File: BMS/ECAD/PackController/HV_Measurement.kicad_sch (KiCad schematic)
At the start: 0 parts

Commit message: implement HV measurement
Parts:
- added C28, C29, C30, C35, C40, C41: 1uC 0805 50V, symbol Device:C
- added C31, C39, C42: 100n 0603 50V, symbol Device:C
- added C32, C36: 100nF 0603 100V, Capacitor_SMD:C_0603_1608Metric_Pad1.08x0.95mm_HandSolder, symbol Device:C
- added C33, C34, C37, C38: 10uF 0805 50V, Capacitor_SMD:C_0805_2012Metric, symbol Device:C
- added R49, R59, R63, R64: 4.7MR 2512 3kV 1%, symbol Device:R
- added R60: 55.6kR 2512 500V 1%, symbol Device:R
- added R61, R62, R66, R67, R70: 10kR, Resistor_SMD:R_0603_1608Metric_Pad0.98x0.95mm_HandSolder, symbol Device:R
- added R65: 39kR 2512 500V 1%, symbol Device:R
- added R68: 68K 1%, Resistor_SMD:R_0603_1608Metric_Pad0.98x0.95mm_HandSolder, symbol Device:R
- added R69: 3.3k 1%, Resistor_SMD:R_0603_1608Metric_Pad0.98x0.95mm_HandSolder, symbol Device:R
- added U10, U12: (no value), symbol EKartParts:ADUM3190
- added U11, U13: TEA1-0505HI, Converter_DCDC:Converter_DCDC_TRACO_TEA1-xxxxHI_THT, symbol Converter_DCDC:TEA1-0505HI
- added U14: (no value), symbol EKartParts:ADCMP393ARUZ
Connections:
- new net: C38.2, U13.2 (-Vin)
- new net: C35.1, U12.14 (VREG2)
- new net: R61.1, R62.2, U10.6 (EAOUT2)
- new net: C28.1, U10.14 (VREG2)
- new net: C34.2, U11.2 (-Vin)
- new net: C32.1, C33.2, U11.5 (-Vout)
- new net: R63.2, R64.1
- new net: C36.1, C37.2, U13.5 (-Vout)
- new net: C30.1, U10.3 (VREG1)
- new net: R68.2, R69.1, U14.5 (+)
- new net: C42.1, U14.3 (VCC)
- new net: R66.1, R67.2, U12.6 (EAOUT2)
- new net: R49.2, R59.1
- new net: U12.10 (COMP), U12.11 (-In)
- new net: C40.1, U12.3 (VREG1)
- new net: U10.10 (COMP), U10.11 (-In)
- new net +3.3V: C29.1, C41.1, R61.2, R66.2, R68.1, R70.1, U10.1 (VDD1), U12.1 (VDD1)
- new net +5V: C34.1, C38.1, U11.1 (+Vin), U13.1 (+Vin)
- new net +5V_ACCU: C36.2, C37.1, U12.16 (VDD2), U13.7 (+Vout)
- new net +5V_VEHI: C32.2, C33.1, U10.16 (VDD2), U11.7 (+Vout)
- new net DANGER_V: R70.2, U14.2
- new net GND: C29.2, C30.2, C31.2, C39.2, C40.2, C41.2, C42.2, R69.2, U10.2 (GND1), U10.8 (GND1), U12.2 (GND1), U12.8 (GND1), U14.12 (GND)
- new net TS_P_ACCU: C35.2, R63.1, R64.2, R65.1, R65.2, U12.12 (+IN), U12.15 (GND2), U12.9 (GND2)
- new net TS_P_VEHI: C28.2, R49.1, R59.2, R60.1, R60.2, U10.12 (+IN), U10.15 (GND2), U10.9 (GND2)
- new net V_ACCU: C39.1, R67.1
- new net V_VEHI: C31.1, R62.1, U14.4 (-)
- no-connect marks 0 -> 6

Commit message: schematic finished, review tbd
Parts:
- removed unit 4 of U14
- removed unit 3 of U14
- added R76: 68K 1%, Resistor_SMD:R_0603_1608Metric_Pad0.98x0.95mm_HandSolder, symbol Device:R
- added R82: 3.3k 1%, Resistor_SMD:R_0603_1608Metric_Pad0.98x0.95mm_HandSolder, symbol Device:R
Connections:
- net +3.3V: now also R76.1
- net DANGER_V: now also U14.1; no longer R70.2, U14.2
- net GND: now also R82.2
- net TS_P_ACCU: no longer C35.2, R64.2, R65.1, R65.2, U12.12 (+IN), U12.15 (GND2), U12.9 (GND2)
- net TS_P_VEHI: no longer C28.2, R59.2, R60.1, R60.2, U10.12 (+IN), U10.15 (GND2), U10.9 (GND2)
- net V_VEHI: now also U14.7 (+)
- net TS_N_VEHI: now reaches C32.1, C33.2, U11.5 (-Vout)
- net TS_N_VEHI: now also C28.2, R59.2, R60.1, R60.2, U10.12 (+IN), U10.15 (GND2), U10.9 (GND2)
- net TS_N_ACCU: now reaches C36.1, C37.2, U13.5 (-Vout)
- net TS_N_ACCU: now also C35.2, R64.2, R65.1, R65.2, U12.12 (+IN), U12.15 (GND2), U12.9 (GND2)
- net at U14.6 (-): now also R76.2, R82.1
- new net nDANGER_V: R70.2, U14.2
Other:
- moved on the sheet: C42, R68, R69, R70, U14A, U14E

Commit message: close to finish BMS master, only some footprints needed
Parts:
- removed C40, C41: 1uC 0805 50V, symbol Device:C
- removed R49, R59, R63, R64: 4.7MR 2512 3kV 1%, symbol Device:R
- removed R60: 55.6kR 2512 500V 1%, symbol Device:R
- removed R65: 39kR 2512 500V 1%, symbol Device:R
- added C910, C911: 1uC 0805 50V, Capacitor_SMD:C_0805_2012Metric, symbol Device:C
- added R902, R904, R907, R911: 4.7MR 2512 3kV 1%, Resistor_SMD:R_2512_6332Metric_Pad1.40x3.35mm_HandSolder, symbol Device:R
- added R912, R916: 39kR 2512 500V 1%, symbol Device:R
- C903: renamed from C30; footprint (none) -> Capacitor_SMD:C_0805_2012Metric
- C904: renamed from C29; footprint (none) -> Capacitor_SMD:C_0805_2012Metric
- renumbered C42 to C901, C28 to C902, C31 to C905, C32 to C906, C33 to C907, C34 to C908, C35 to C909, C39 to C912, C36 to C913, C37 to C914, C38 to C915, R76 to R901, R82 to R903, R61 to R905, R62 to R906, R68 to R908, R70 to R909, R69 to R910, R66 to R913, R67 to R914, U14 to U901, U10 to U902, U11 to U903, U12 to U904, U13 to U905
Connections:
- net +3.3V: now also C911.1
- net GND: now also C910.2, C911.2
- net TS_N_ACCU: now also R911.2, R912.1, R912.2
- net TS_N_VEHI: now also R904.2, R916.1, R916.2
- net TS_P_ACCU: now also R907.1
- net TS_P_VEHI: now also R902.1
- net at U904.3 (VREG1): now also C910.1
- new net: R907.2, R911.1
- new net: R902.2, R904.1

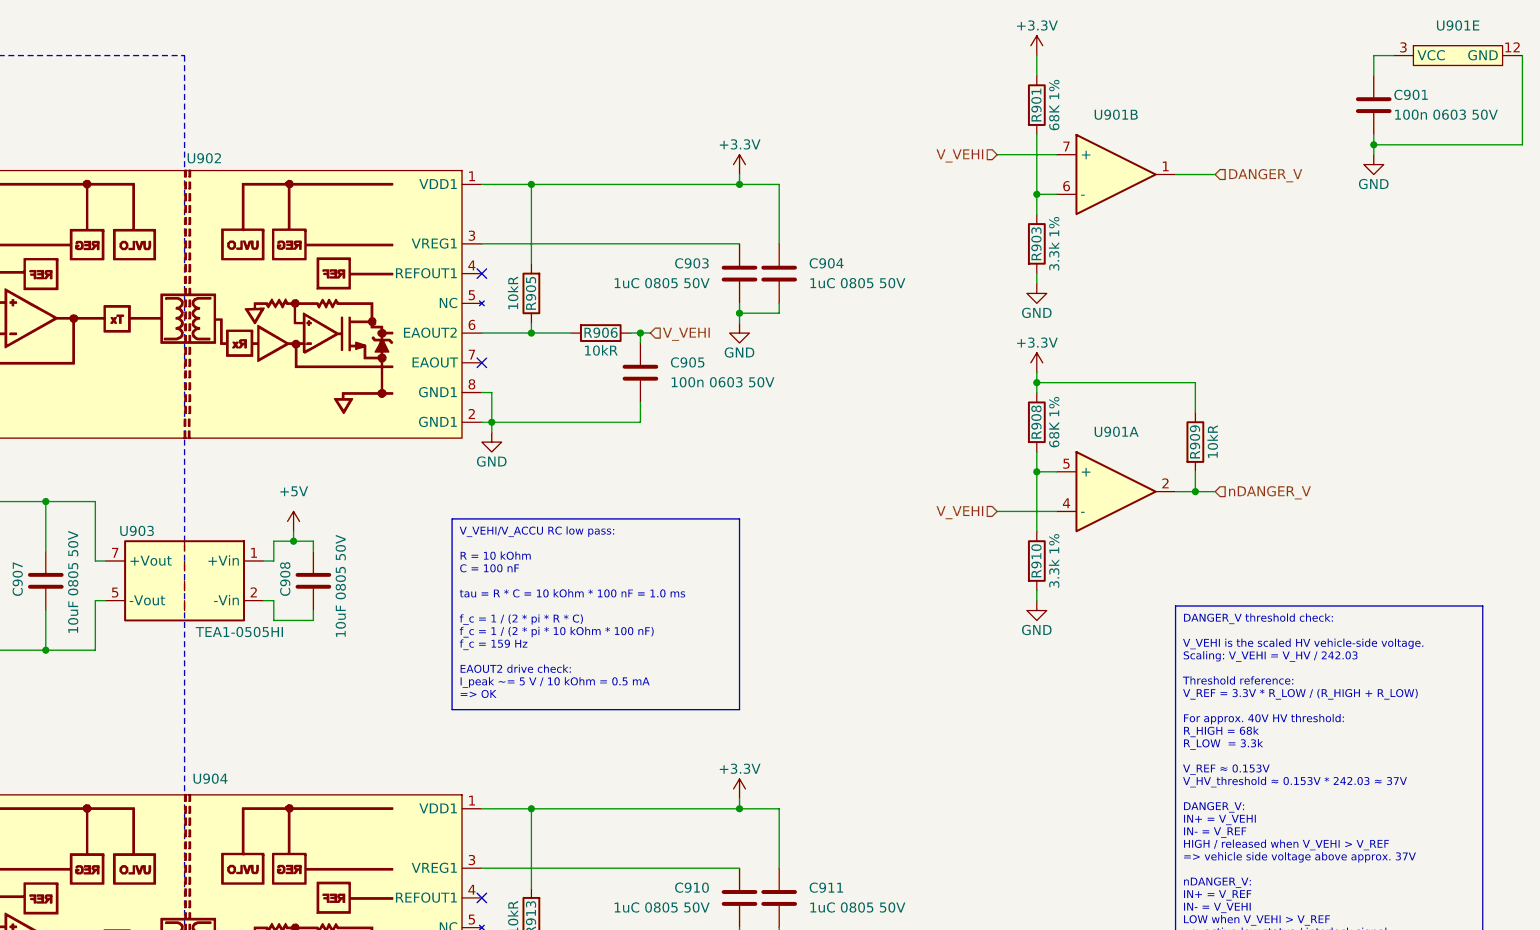
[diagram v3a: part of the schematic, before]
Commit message: finalised schematic of pack controller
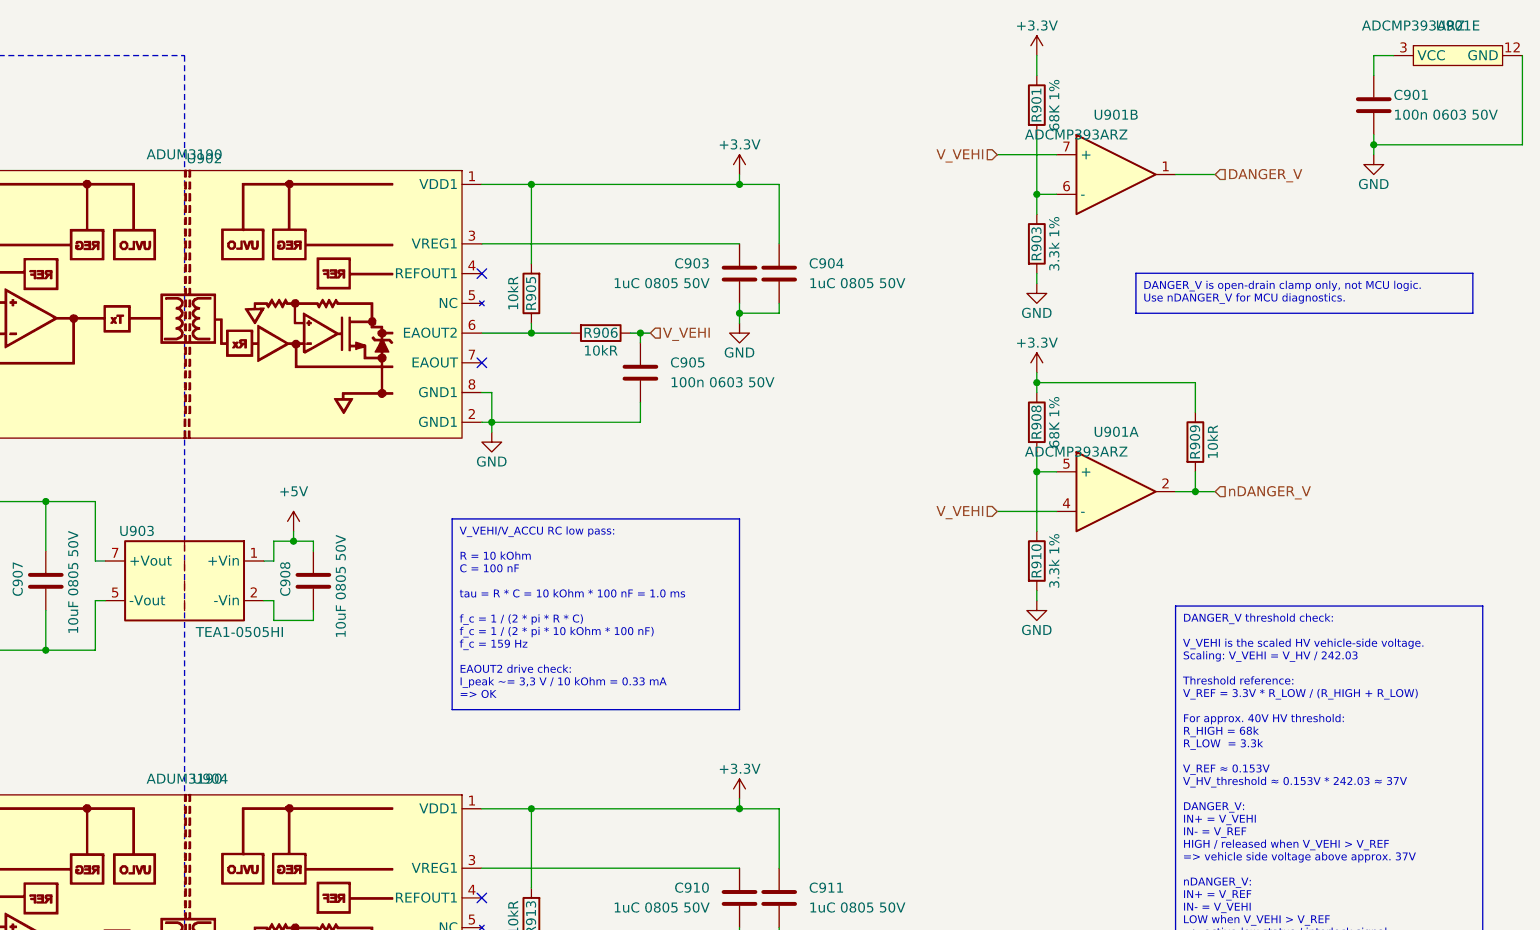
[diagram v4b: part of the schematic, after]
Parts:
- C901, C905, C912: footprint (none) -> Capacitor_SMD:C_0603_1608Metric
- C902, C909: footprint (none) -> Capacitor_SMD:C_0805_2012Metric
- R912, R916: footprint (none) -> Resistor_SMD:R_2512_6332Metric_Pad1.40x3.35mm_HandSolder
- U901: value (none) -> ADCMP393ARZ; footprint (none) -> Package_SO:SOIC-14_3.9x8.7mm_P1.27mm
- U902, U904: value (none) -> ADUM3190; footprint (none) -> Package_SO:QSOP-16_3.9x4.9mm_P0.635mm
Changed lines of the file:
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@@
 		)
 	)
-	(text_box "V_VEHI/V_ACCU RC low pass:\n\nR = 10 kOhm\nC = 100 nF\n\ntau = R * C = 10 kOhm * 100 nF = 1.0 ms\n\nf_c = 1 / (2 * pi * R * C)\nf_c = 1 / (2 * pi * 10 kOhm * 100 nF)\nf_c = 159 Hz\n\nEAOUT2 drive check:\nI_peak ~= 5 V / 10 kOhm = 0.5 mA\n=> OK"
+	(text_box "V_VEHI/V_ACCU RC low pass:\n\nR = 10 kOhm\nC = 100 nF\n\ntau = R * C = 10 kOhm * 100 nF = 1.0 ms\n\nf_c = 1 / (2 * pi * R * C)\nf_c = 1 / (2 * pi * 10 kOhm * 100 nF)\nf_c = 159 Hz\n\nEAOUT2 drive check:\nI_peak ~= 3,3 V / 10 kOhm = 0.33 mA\n=> OK"
 		(exclude_from_sim no)
 		(at 142.24 78.4269 0)
@@
 		)
 	)
+	(text_box "DANGER_V is open-drain clamp only, not MCU logic.\nUse nDANGER_V for MCU diagnostics."
+		(exclude_from_sim no)
+		(at 229.87 46.9463 0)
+		(size 43.18 5.1237)
+		(margins 0.9525 0.9525 0.9525 0.9525)
+		(stroke
+			(width 0)
+			(type solid)
+			(color 0 0 0 1)
+		)
+		(fill
+			(type color)
+			(color 255 255 194 1)
+		)
+		(effects
+			(font
+				(size 1 1)
+				(color 0 0 0 1)
+			)
+			(justify left top)
+		)
+	)
 	(junction
 		(at 179.07 35.56)
@@
 			)
 		)
-		(property "Footprint" ""
+		(property "Footprint" "Capacitor_SMD:C_0805_2012Metric"
 			(at 65.0748 130.81 0)
 			(hide yes)
@@
 			)
 		)
-		(property "Footprint" ""
+		(property "Footprint" "Capacitor_SMD:C_0805_2012Metric"
 			(at 65.0748 50.8 0)
 			(hide yes)
@@
 			)
 		)
-		(property "Footprint" ""
+		(property "Footprint" "Resistor_SMD:R_2512_6332Metric_Pad1.40x3.35mm_HandSolder"
 			(at 42.672 135.89 90)
 			(hide yes)
@@
 			)
 		)
-		(property "Value" ""
+		(property "Value" "ADCMP393ARZ"
 			(at 265.43 15.24 0)
 			(show_name no)
@@
 			)
 		)
-		(property "Footprint" ""
+		(property "Footprint" "Package_SO:SOIC-14_3.9x8.7mm_P1.27mm"
 			(at 265.43 15.24 0)
 			(hide yes)
@@
 			)
 		)
-		(property "Datasheet" ""
+		(property "Datasheet" "https://www.analog.com/media/en/technical-documentation/data-sheets/ADCMP391_392_393.pdf"
 			(at 265.43 15.24 0)
 			(hide yes)
@@
 			)
 		)
-		(property "Footprint" ""
+		(property "Footprint" "Capacitor_SMD:C_0603_1608Metric"
 			(at 167.3352 63.5 0)
 			(hide yes)
@@
 			)
 		)
-		(property "Value" ""
+		(property "Value" "ADUM3190"
 			(at 107.95 111.76 0)
 			(show_name no)
@@
 			)
 		)
-		(property "Footprint" ""
+		(property "Footprint" "Package_SO:QSOP-16_3.9x4.9mm_P0.635mm"
 			(at 107.95 111.76 0)
 			(hide yes)
@@
 			)
 		)
-		(property "Footprint" ""
+		(property "Footprint" "Resistor_SMD:R_2512_6332Metric_Pad1.40x3.35mm_HandSolder"
 			(at 42.672 55.88 90)
 			(hide yes)
@@
 			)
 		)
-		(property "Value" ""
+		(property "Value" "ADUM3190"
 			(at 107.95 31.75 0)
 			(show_name no)
@@
 			)
 		)
-		(property "Footprint" ""
+		(property "Footprint" "Package_SO:QSOP-16_3.9x4.9mm_P0.635mm"
 			(at 107.95 31.75 0)
 			(hide yes)
@@
 			)
 		)
-		(property "Datasheet" ""
+		(property "Datasheet" "https://www.analog.com/media/en/technical-documentation/data-sheets/ADuM3190.pdf"
 			(at 107.95 31.75 0)
 			(hide yes)
@@
 			)
 		)
-		(property "Footprint" ""
+		(property "Footprint" "Capacitor_SMD:C_0603_1608Metric"
 			(at 167.3352 143.51 0)
 			(hide yes)
@@
 			)
 		)
-		(property "Value" ""
+		(property "Value" "ADCMP393ARZ"
 			(at 222.25 69.85 0)
 			(show_name no)
@@
 			)
 		)
-		(property "Footprint" ""
+		(property "Footprint" "Package_SO:SOIC-14_3.9x8.7mm_P1.27mm"
 			(at 222.25 69.85 0)
 			(hide yes)
@@
 			)
 		)
-		(property "Datasheet" ""
+		(property "Datasheet" "https://www.analog.com/media/en/technical-documentation/data-sheets/ADCMP391_392_393.pdf"
 			(at 222.25 69.85 0)
 			(hide yes)
@@
 			)
 		)
-		(property "Value" ""
+		(property "Value" "ADCMP393ARZ"
 			(at 222.25 29.21 0)
 			(show_name no)
@@
 			)
 		)
-		(property "Footprint" ""
+		(property "Footprint" "Package_SO:SOIC-14_3.9x8.7mm_P1.27mm"
 			(at 222.25 29.21 0)
 			(hide yes)
@@
 			)
 		)
-		(property "Datasheet" ""
+		(property "Datasheet" "https://www.analog.com/media/en/technical-documentation/data-sheets/ADCMP391_392_393.pdf"
 			(at 222.25 29.21 0)
 			(hide yes)
@@
 			)
 		)
-		(property "Footprint" ""
+		(property "Footprint" "Capacitor_SMD:C_0603_1608Metric"
 			(at 261.3152 29.21 0)
 			(hide yes)

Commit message: many fixes
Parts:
- removed C902, C903, C904, C909, C910, C911: 1uC 0805 50V, Capacitor_SMD:C_0805_2012Metric, symbol Device:C
- removed C905, C912: 100n 0603 50V, Capacitor_SMD:C_0603_1608Metric, symbol Device:C
- removed C906, C913: 100nF 0603 100V, Capacitor_SMD:C_0603_1608Metric_Pad1.08x0.95mm_HandSolder, symbol Device:C
- removed C907, C908, C914, C915: 10uF 0805 50V, Capacitor_SMD:C_0805_2012Metric, symbol Device:C
- removed R905, R906, R913, R914: 10kR, Resistor_SMD:R_0603_1608Metric_Pad0.98x0.95mm_HandSolder, symbol Device:R
- removed R907, R911: 4.7MR 2512 3kV 1%, Resistor_SMD:R_2512_6332Metric_Pad1.40x3.35mm_HandSolder, symbol Device:R
- removed R912, R916: 39kR 2512 500V 1%, Resistor_SMD:R_2512_6332Metric_Pad1.40x3.35mm_HandSolder, symbol Device:R
- removed U902, U904: ADUM3190, Package_SO:QSOP-16_3.9x4.9mm_P0.635mm, symbol EKartParts:ADUM3190
- removed U903, U905: TEA1-0505HI, Converter_DCDC:Converter_DCDC_TRACO_TEA1-xxxxHI_THT, symbol Converter_DCDC:TEA1-0505HI
- added C916, C919, C928, C931: 100nF 0603 100V, Capacitor_SMD:C_0603_1608Metric_Pad1.08x0.95mm_HandSolder, symbol Device:C
- added C917, C929: 1uF 0805 50V, Capacitor_SMD:C_0805_2012Metric, symbol Device:C
- added C918, C930: 100pC 0603 50V, Capacitor_SMD:C_0603_1608Metric, symbol Device:C
- added C920, C932: 1uC 0805 50V, Capacitor_SMD:C_0805_2012Metric, symbol Device:C
- added C921, C926, C933, C938: 100nC 0603 50V, Capacitor_SMD:C_0603_1608Metric, symbol Device:C
- added C922, C923, C934, C935: 10uF 0805 50V, Capacitor_SMD:C_0805_2012Metric, symbol Device:C
- added C924, C936: 100nC 0603 16V, Capacitor_SMD:C_0603_1608Metric, symbol Device:C
- added C925, C937: 1uC 0805 16V, Capacitor_SMD:C_0805_2012Metric, symbol Device:C
- added C927, C939: 1nC 0603 16V, Capacitor_SMD:C_0603_1608Metric, symbol Device:C
- added R915, R917: 100kR 0.1%, Resistor_SMD:R_0603_1608Metric_Pad0.98x0.95mm_HandSolder, symbol Device:R
- added R918, R919: 909kR 0.1%, Resistor_SMD:R_0603_1608Metric_Pad0.98x0.95mm_HandSolder, symbol Device:R
- added R920: 10kR, Resistor_SMD:R_0603_1608Metric_Pad0.98x0.95mm_HandSolder, symbol Device:R
- added R921, R922, R925, R926: 4.7MR 2512 3kV 0,1%, Resistor_SMD:R_2512_6332Metric_Pad1.40x3.35mm_HandSolder, symbol Device:R
- added R923, R927: 26.1kR 2512 500V 0,1%, Resistor_SMD:R_2512_6332Metric_Pad1.40x3.35mm_HandSolder, symbol Device:R
- added R924, R928: 1kR, Resistor_SMD:R_0603_1608Metric_Pad0.98x0.95mm_HandSolder, symbol Device:R
- added unit 4 of U901
- added unit 3 of U901
- added U906, U909: LP5907MFX-3.3, Package_TO_SOT_SMD:SOT-23-5, symbol Regulator_Linear:LP5907MFX-3.3
- added U907, U910: AMC0311R, EKartParts:AMC0311R Wide-body SOIC (DWV), symbol EKartParts:AMC0311R
- added U908, U911: TEA1-0505HI, Converter_DCDC:Converter_DCDC_TRACO_TEA1-xxxxHI_THT, symbol Converter_DCDC:TEA1-0505HI
- R901: value 68K 1% -> 68.1K 0.1%
- R902, R904: value 4.7MR 2512 3kV 1% -> 500R 0805; footprint Resistor_SMD:R_2512_6332Metric_Pad1.40x3.35mm_HandSolder -> Resistor_SMD:R_0805_2012Metric_Pad1.20x1.40mm_HandSolder
- R903, R910: value 3.3k 1% -> 3.9k 0.1%
- R908: value 68K 1% -> 68,1K 0.1%
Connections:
- net +3.3V: now also C901.1, U901.3 (VCC), C926.1, C938.1, R920.1, U907.6 (REFIN), U910.6 (REFIN)
- net +5V: now also C923.1, C924.1, C925.1, C935.1, C936.1, C937.1, U907.8 (VDD2), U908.1 (+Vin), U910.8 (VDD2), U911.1 (+Vin)
- net +5V_ACCU: now also R902.2, C919.2, C922.1, U906.1 (IN), U906.3 (EN), U908.7 (+Vout)
- net +5V_VEHI: now also R904.2, C931.2, C934.1, U909.1 (IN), U909.3 (EN), U911.7 (+Vout)
- net GND: now also C923.2, C924.2, C925.2, C926.2, C927.2, C935.2, C936.2, C937.2, C938.2, C939.2, R918.2, R919.2, U907.5 (GND2), U908.2 (-Vin), U910.5 (GND2), U911.2 (-Vin)
- net TS_N_ACCU: now also R902.1, C916.1, C917.2, C918.2, C919.1, C920.2, C921.2, C922.2, R923.2, U906.2 (GND), U907.3 (SNSN), U907.4 (GND1), U908.5 (-Vout)
- net TS_N_VEHI: now also R904.1, C928.1, C929.2, C930.2, C931.1, C932.2, C933.2, C934.2, R927.2, U909.2 (GND), U910.3 (SNSN), U910.4 (GND1), U911.5 (-Vout); no longer R904.2
- net TS_P_ACCU: now also R921.1
- net TS_P_VEHI: now also R925.1; no longer R902.1
- net V_ACCU: now also C927.1, R915.1, R917.1, R924.1
- net V_VEHI: now also C939.1, R928.1, U901.10 (-), U901.9 (+)
- net DANGER_V renamed DANGER_V_oD
- new net: C918.1, R922.2, R923.1, U907.2 (INP)
- new net: R925.2, R926.1
- new net: C930.1, R926.2, R927.1, U910.2 (INP)
- new net: R924.2, U907.7 (OUT)
- new net: R917.2, R919.1, U901.8 (-)
- new net: R915.2, R918.1, U901.11 (+)
- new net: R928.2, U910.7 (OUT)
- new net: R921.2, R922.1
- new net +3.3V_ACCU: C916.2, C917.1, C920.1, C921.1, U906.5 (OUT), U907.1 (VDD1)
- new net +3.3V_VEHI: C928.2, C929.1, C932.1, C933.1, U909.5 (OUT), U910.1 (VDD1)
- new net PRCHG_DONE: U901.14
- new net nPRCHG_DONE: R920.2, U901.13
- no-connect marks 6 -> 0
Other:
- moved on the sheet: C901, R901, R903, R908, R909, R910, U901A, U901B, U901E
